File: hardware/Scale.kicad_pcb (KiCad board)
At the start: 2 copper layers, 45 x 45 mm, 161 parts, among them J1 Load Cell Connector, J2 GPIO, J3 RS232, J4 DebugEdge_02x03, J5 Display Connector, J7 12401610E4#2A, Q1 DMG2307L, Q2 DMG2307L, Q3 BSD235N, SW1 RESET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

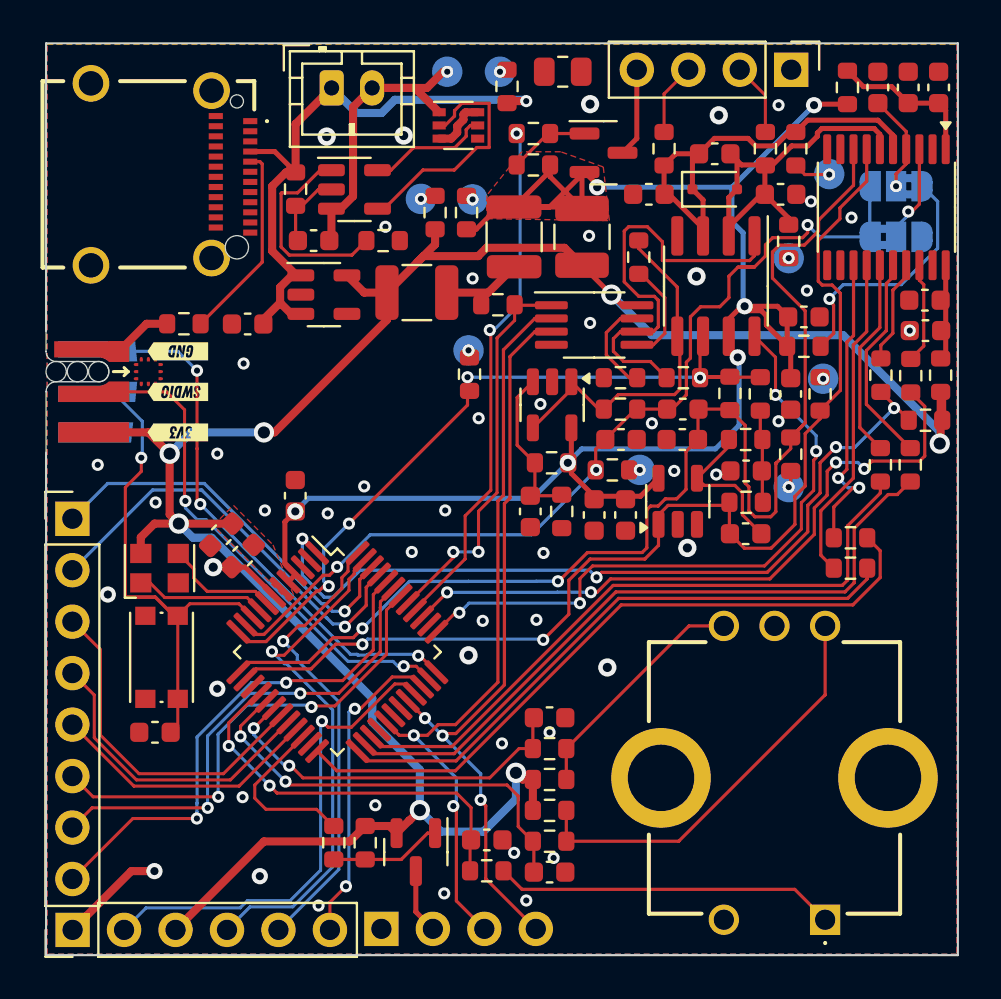
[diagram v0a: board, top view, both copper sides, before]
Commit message: Move board edge for manufacturing
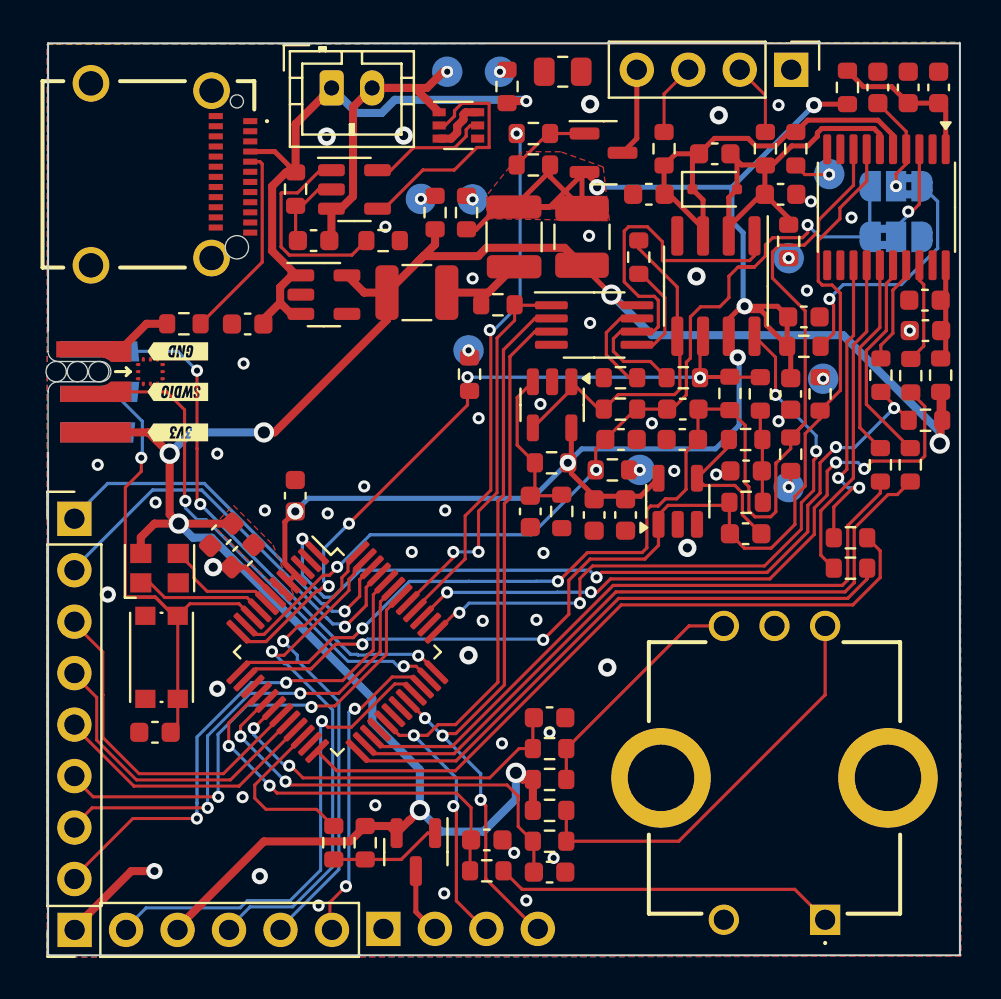
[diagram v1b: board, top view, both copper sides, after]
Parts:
- moved J2 0.10 mm to (114.7, 69.9)
- moved J3 0.10 mm to (114.7, 90.2)
- moved J4 0.10 mm to (113.3, 63.6)
- moved J5 0.10 mm to (129.9, 90.2)
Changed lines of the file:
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@@
 		(locked yes)
 		(layer "F.Cu")
-		(at 113.25 63.65 -90)
+		(at 113.35 63.65 -90)
 		(property "Reference" "J4"
 			(at 0 1.2 270)
@@
 		(locked yes)
 		(layer "F.Cu")
-		(at 114.55 69.91)
+		(at 114.65 69.91)
 		(descr "Through hole straight pin header, 1x08, 2.54mm pitch, single row")
 		(tags "Through hole pin header THT 1x08 2.54mm single row")
@@
 		(locked yes)
 		(layer "F.Cu")
-		(at 114.56 90.2 90)
+		(at 114.66 90.2 90)
 		(descr "Through hole straight pin header, 1x06, 2.54mm pitch, single row")
 		(tags "Through hole pin header THT 1x06 2.54mm single row")
@@
 		(locked yes)
 		(layer "B.Cu")
-		(at 129.8 90.15 -90)
+		(at 129.9 90.15 -90)
 		(descr "Through hole straight pin header, 1x04, 2.54mm pitch, single row")
 		(tags "Through hole pin header THT 1x04 2.54mm single row")
@@
 	)
 	(gr_line
-		(start 113.25 46.45)
-		(end 113.25 60.65)
+		(start 113.35 46.45)
+		(end 113.35 60.65)
 		(stroke
 			(width 0.1)
@@
 	)
 	(gr_line
-		(start 158.25 91.45)
-		(end 158.25 46.45)
+		(start 158.35 91.45)
+		(end 158.35 46.45)
 		(stroke
 			(width 0.1)
@@
 	)
 	(gr_line
-		(start 113.25 46.45)
-		(end 158.25 46.45)
+		(start 113.35 46.45)
+		(end 158.35 46.45)
 		(stroke
 			(width 0.1)
@@
 	)
 	(gr_line
-		(start 113.25 91.45)
-		(end 158.25 91.45)
+		(start 113.35 91.45)
+		(end 158.35 91.45)
 		(stroke
 			(width 0.1)
@@
 	)
 	(gr_line
-		(start 113.25 66.65)
-		(end 113.25 91.45)
+		(start 113.35 66.65)
+		(end 113.35 91.45)
 		(stroke
 			(width 0.1)
@@
 	)
 	(segment
+		(start 122.004768 82.4942)
+		(end 117.839132 82.4942)
+		(width 0.1524)
+		(layer "F.Cu")
+		(net 31)
+	)
+	(segment
 		(start 117.839132 82.4942)
-		(end 115.9354 80.590468)
+		(end 116.0558 80.710868)
 		(width 0.1524)
 		(layer "F.Cu")
@@
 	)
 	(segment
-		(start 115.9354 76.3754)
-		(end 114.55 74.99)
+		(start 116.0558 78.603333)
+		(end 116.05 78.597534)
 		(width 0.1524)
 		(layer "F.Cu")
@@
 	)
 	(segment
-		(start 115.9354 80.590468)
-		(end 115.9354 76.3754)
+		(start 124.859783 79.639185)
+		(end 122.004768 82.4942)
 		(width 0.1524)
 		(layer "F.Cu")
@@
 	)
 	(segment
-		(start 122.004768 82.4942)
-		(end 117.839132 82.4942)
+		(start 116.05 76.49)
+		(end 114.55 74.99)
 		(width 0.1524)
 		(layer "F.Cu")
@@
 	)
 	(segment
-		(start 124.859783 79.639185)
-		(end 122.004768 82.4942)
+		(start 116.0558 80.710868)
+		(end 116.0558 78.603333)
 		(width 0.1524)
 		(layer "F.Cu")
@@
 	)
 	(segment
-		(start 117.712466 82.8)
-		(end 122.348629 82.8)
+		(start 116.05 78.597534)
+		(end 116.05 76.49)
 		(width 0.1524)
 		(layer "F.Cu")
-		(net 32)
+		(net 31)
 	)
 	(segment
@@
 	(segment
 		(start 114.55 77.53)
-		(end 115.6296 78.6096)
+		(end 115.75 78.73)
 		(width 0.1524)
 		(layer "F.Cu")
@@
 	)
 	(segment
-		(start 115.6296 78.6096)
-		(end 115.6296 80.717134)
+		(start 117.712466 82.8)
+		(end 122.348629 82.8)
 		(width 0.1524)
 		(layer "F.Cu")
@@
 	)
 	(segment
-		(start 115.6296 80.717134)
+		(start 115.75 80.837534)
 		(end 117.712466 82.8)
 		(width 0.1524)
@@
 	)
 	(segment
+		(start 115.75 78.73)
+		(end 115.75 80.837534)
+		(width 0.1524)
+		(layer "F.Cu")
+		(net 32)
+	)
+	(segment
 		(start 117.5858 83.1058)
 		(end 114.55 80.07)
@@
 		(min_thickness 0.16)
 		(filled_areas_thickness no)
-		(fill yes
+		(fill
 			(thermal_gap 0.5)
 			(thermal_bridge_width 0.5)
@@
 		(polygon
 			(pts
-				(xy 113.3 46.5) (xy 158.2 46.5) (xy 158.2 91.4) (xy 113.3 91.4)
+				(xy 113.3 46.5) (xy 158.35 46.4) (xy 158.4 91.5) (xy 113.3 91.55)
 			)
 		)

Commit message: Added net classes
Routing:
- net /Display/SCL: track 37.5 -> 37.0 mm
